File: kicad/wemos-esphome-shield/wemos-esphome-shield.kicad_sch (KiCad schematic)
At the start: 27 parts, among them Q1 2N2219, Q2 2N2219, Q3 2N2219, T1 Transformer_1P_1S, U1 WeMos_D1_mini

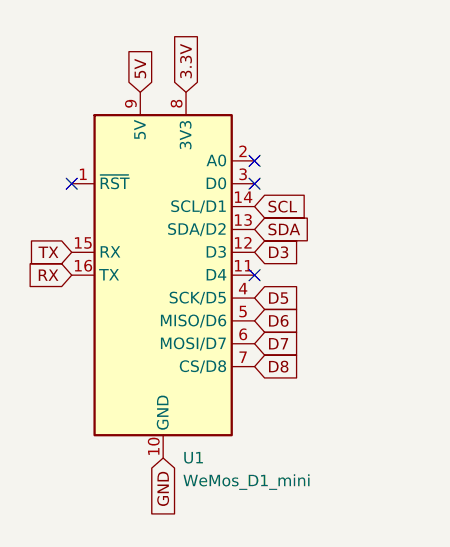
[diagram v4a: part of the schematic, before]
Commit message: first positioning of footprints
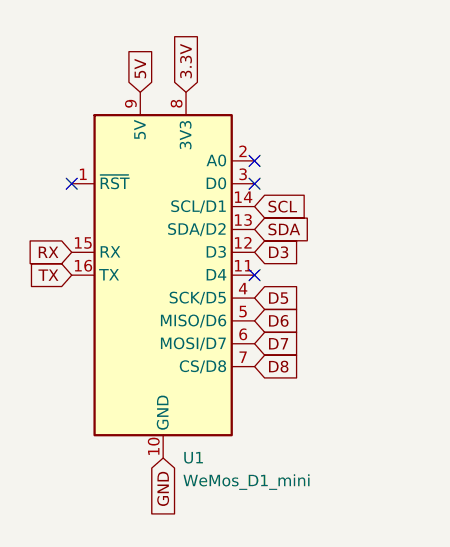
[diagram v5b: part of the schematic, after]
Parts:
- GEST1: footprint (none) -> internal:APDS9960
- LED1: footprint internal:LED ring -> internal:LED breakout
- LUM1: footprint internal:TEMT6000 -> internal:BH1750
- MOV1: footprint (none) -> internal:LD2410C
- OLED2: footprint internal:SSD1306 OLED 128x32 -> internal:SSD1306 OLED 128x64
- Q1, Q2, Q3: footprint Package_TO_SOT_THT:TO-92L_Inline -> Package_TO_SOT_SMD:SOT-23_Handsoldering
- R1, R5: footprint Resistor_THT:R_Axial_DIN0207_L6.3mm_D2.5mm_P10.16mm_Horizontal -> Resistor_SMD:R_1206_3216Metric_Pad1.30x1.75mm_HandSolder
- R2, R3, R4, R6, R7, R8: footprint (none) -> Resistor_SMD:R_1206_3216Metric_Pad1.30x1.75mm_HandSolder
- TEMP1: footprint Connector_JST:JST_XH_B4B-XH-AM_1x04_P2.50mm_Vertical -> Connector_JST:JST_XH_B4B-XH-A_1x04_P2.50mm_Vertical
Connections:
- net RX: now also U1.15 (RX); no longer U1.16 (TX)
- net TX: now also U1.16 (TX); no longer U1.15 (RX)
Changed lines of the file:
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@@
     )
   )
-  (global_label "TX" (shape input) (at 35.56 38.1 180) (fields_autoplaced)
-    (effects (font (size 1.27 1.27)) (justify right))
-    (property "Intersheetrefs" "${INTERSHEET_REFS}" (at 30.3977 38.1 0)
+  (global_label "TX" (shape input) (at 35.56 40.64 180) (fields_autoplaced)
+    (effects (font (size 1.27 1.27)) (justify right))
+    (property "Intersheetrefs" "${INTERSHEET_REFS}" (at 30.3977 40.64 0)
       (effects (font (size 1.27 1.27)) (justify right) hide)
     )
@@
     )
   )
-  (global_label "RX" (shape input) (at 35.56 40.64 180) (fields_autoplaced)
-    (effects (font (size 1.27 1.27)) (justify right))
-    (property "Intersheetrefs" "${INTERSHEET_REFS}" (at 30.0953 40.64 0)
+  (global_label "RX" (shape input) (at 35.56 38.1 180) (fields_autoplaced)
+    (effects (font (size 1.27 1.27)) (justify right))
+    (property "Intersheetrefs" "${INTERSHEET_REFS}" (at 30.0953 38.1 0)
       (effects (font (size 1.27 1.27)) (justify right) hide)
     )
@@
       (effects (font (size 1.27 1.27)) (justify right))
     )
-    (property "Footprint" "" (at 173.99 58.42 0)
+    (property "Footprint" "internal:LD2410C" (at 173.99 58.42 0)
       (effects (font (size 1.27 1.27)) hide)
     )
@@
       (effects (font (size 1.27 1.27)))
     )
-    (property "Footprint" "Resistor_THT:R_Axial_DIN0207_L6.3mm_D2.5mm_P10.16mm_Horizontal" (at 53.34 124.46 0)
+    (property "Footprint" "Resistor_SMD:R_1206_3216Metric_Pad1.30x1.75mm_HandSolder" (at 53.34 124.46 0)
       (effects (font (size 1.27 1.27)) hide)
     )
@@
       (effects (font (size 1.27 1.27)) (justify left))
     )
-    (property "Footprint" "Package_TO_SOT_THT:TO-92L_Inline" (at 76.2 126.365 0)
+    (property "Footprint" "Package_TO_SOT_SMD:SOT-23_Handsoldering" (at 76.2 126.365 0)
       (effects (font (size 1.27 1.27) italic) (justify left) hide)
     )
@@
       (effects (font (size 1.27 1.27)))
     )
-    (property "Footprint" "" (at 132.08 134.62 0)
+    (property "Footprint" "Resistor_SMD:R_1206_3216Metric_Pad1.30x1.75mm_HandSolder" (at 132.08 134.62 0)
       (effects (font (size 1.27 1.27)) hide)
     )
@@
       (effects (font (size 1.27 1.27)) (justify right))
     )
-    (property "Footprint" "" (at 198.12 63.5 0)
+    (property "Footprint" "internal:APDS9960" (at 198.12 63.5 0)
       (effects (font (size 1.27 1.27)) hide)
     )
@@
       (effects (font (size 1.27 1.27)))
     )
-    (property "Footprint" "" (at 62.23 97.79 0)
+    (property "Footprint" "Resistor_SMD:R_1206_3216Metric_Pad1.30x1.75mm_HandSolder" (at 62.23 97.79 0)
       (effects (font (size 1.27 1.27)) hide)
     )
@@
       (effects (font (size 1.27 1.27)))
     )
-    (property "Footprint" "" (at 124.46 124.46 0)
+    (property "Footprint" "Resistor_SMD:R_1206_3216Metric_Pad1.30x1.75mm_HandSolder" (at 124.46 124.46 0)
       (effects (font (size 1.27 1.27)) hide)
     )
@@
       (effects (font (size 1.27 1.27)))
     )
-    (property "Footprint" "" (at 125.73 109.22 0)
+    (property "Footprint" "Resistor_SMD:R_1206_3216Metric_Pad1.30x1.75mm_HandSolder" (at 125.73 109.22 0)
       (effects (font (size 1.27 1.27)) hide)
     )
@@
       (effects (font (size 1.27 1.27)))
     )
-    (property "Footprint" "Connector_JST:JST_XH_B4B-XH-AM_1x04_P2.50mm_Vertical" (at 173.99 77.47 0)
+    (property "Footprint" "Connector_JST:JST_XH_B4B-XH-A_1x04_P2.50mm_Vertical" (at 173.99 77.47 0)
       (effects (font (size 1.27 1.27)) hide)
     )
@@
       (effects (font (size 1.27 1.27)))
     )
-    (property "Footprint" "Resistor_THT:R_Axial_DIN0207_L6.3mm_D2.5mm_P10.16mm_Horizontal" (at 53.34 88.9 0)
+    (property "Footprint" "Resistor_SMD:R_1206_3216Metric_Pad1.30x1.75mm_HandSolder" (at 53.34 88.9 0)
       (effects (font (size 1.27 1.27)) hide)
     )
@@
       (effects (font (size 1.27 1.27)))
     )
-    (property "Footprint" "" (at 125.73 116.84 0)
+    (property "Footprint" "Resistor_SMD:R_1206_3216Metric_Pad1.30x1.75mm_HandSolder" (at 125.73 116.84 0)
       (effects (font (size 1.27 1.27)) hide)
     )
@@
       (effects (font (size 1.27 1.27)))
     )
-    (property "Footprint" "" (at 62.23 133.35 0)
+    (property "Footprint" "Resistor_SMD:R_1206_3216Metric_Pad1.30x1.75mm_HandSolder" (at 62.23 133.35 0)
       (effects (font (size 1.27 1.27)) hide)
     )
@@
       (effects (font (size 1.27 1.27)) (justify left))
     )
-    (property "Footprint" "Package_TO_SOT_THT:TO-92L_Inline" (at 76.2 90.805 0)
+    (property "Footprint" "Package_TO_SOT_SMD:SOT-23_Handsoldering" (at 76.2 90.805 0)
       (effects (font (size 1.27 1.27) italic) (justify left) hide)
     )
@@
       (effects (font (size 1.27 1.27)) (justify left))
     )
-    (property "Footprint" "Package_TO_SOT_THT:TO-92L_Inline" (at 139.7 126.365 0)
+    (property "Footprint" "Package_TO_SOT_SMD:SOT-23_Handsoldering" (at 139.7 126.365 0)
       (effects (font (size 1.27 1.27) italic) (justify left) hide)
     )
@@
       (effects (font (size 1.27 1.27)) (justify right))
     )
-    (property "Footprint" "internal:TEMT6000" (at 173.99 93.98 0)
+    (property "Footprint" "internal:BH1750" (at 173.99 93.98 0)
       (effects (font (size 1.27 1.27)) hide)
     )
@@
       (effects (font (size 1.27 1.27)) (justify right))
     )
-    (property "Footprint" "internal:SSD1306 OLED 128x32" (at 198.12 26.67 0)
+    (property "Footprint" "internal:SSD1306 OLED 128x64" (at 198.12 26.67 0)
       (effects (font (size 1.27 1.27)) hide)
     )
@@
       (effects (font (size 1.27 1.27)) (justify right))
     )
-    (property "Footprint" "internal:LED ring" (at 173.99 41.91 0)
-      (effects (font (size 1.27 1.27)) hide)
-    )
+    (property "Footprint" "internal:LED breakout" (at 173.99 41.91 0)
+      (effects (font (size 1.27 1.27)) hide)
+    )

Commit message: wire tracks
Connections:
- net 5V: now also OLED1.3 (Pin_3), OLED2.3 (Pin_3); no longer OLED1.2 (Pin_2), OLED2.2 (Pin_2)
- net GND: now also OLED1.4 (Pin_4), OLED2.4 (Pin_4); no longer OLED1.1 (Pin_1), OLED2.1 (Pin_1)
- net SCL: now also OLED1.2 (Pin_2), OLED2.2 (Pin_2); no longer OLED1.3 (Pin_3), OLED2.3 (Pin_3)
- net SDA: now also OLED1.1 (Pin_1), OLED2.1 (Pin_1); no longer OLED1.4 (Pin_4), OLED2.4 (Pin_4)
- net D8: no longer names the net of U1.7 (CS/D8)
- no-connect marks 9 -> 10
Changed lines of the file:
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@@
   (no_connect (at 55.88 40.64))
   (no_connect (at 55.88 30.48))
+  (no_connect (at 55.88 50.8))
   (no_connect (at 193.04 68.58))
   (no_connect (at 193.04 55.88))
@@
     )
   )
-  (global_label "D8" (shape input) (at 55.88 50.8 0) (fields_autoplaced)
-    (effects (font (size 1.27 1.27)) (justify left))
-    (property "Intersheetrefs" "${INTERSHEET_REFS}" (at 61.3447 50.8 0)
-      (effects (font (size 1.27 1.27)) (justify left) hide)
-    )
-  )
-  (global_label "SCL" (shape input) (at 193.04 24.13 180) (fields_autoplaced)
-    (effects (font (size 1.27 1.27)) (justify right))
-    (property "Intersheetrefs" "${INTERSHEET_REFS}" (at 187.1193 24.2094 0)
+  (global_label "SCL" (shape input) (at 193.04 26.67 180) (fields_autoplaced)
+    (effects (font (size 1.27 1.27)) (justify right))
+    (property "Intersheetrefs" "${INTERSHEET_REFS}" (at 187.1193 26.7494 0)
       (effects (font (size 1.27 1.27)) (justify right) hide)
     )
@@
     )
   )
-  (global_label "5V" (shape input) (at 193.04 26.67 180) (fields_autoplaced)
-    (effects (font (size 1.27 1.27)) (justify right))
-    (property "Intersheetrefs" "${INTERSHEET_REFS}" (at 188.3288 26.5906 0)
-      (effects (font (size 1.27 1.27)) (justify right) hide)
-    )
-  )
-  (global_label "SDA" (shape input) (at 168.91 21.59 180) (fields_autoplaced)
-    (effects (font (size 1.27 1.27)) (justify right))
-    (property "Intersheetrefs" "${INTERSHEET_REFS}" (at 162.9288 21.6694 0)
+  (global_label "5V" (shape input) (at 193.04 24.13 180) (fields_autoplaced)
+    (effects (font (size 1.27 1.27)) (justify right))
+    (property "Intersheetrefs" "${INTERSHEET_REFS}" (at 188.3288 24.0506 0)
+      (effects (font (size 1.27 1.27)) (justify right) hide)
+    )
+  )
+  (global_label "SDA" (shape input) (at 168.91 29.21 180) (fields_autoplaced)
+    (effects (font (size 1.27 1.27)) (justify right))
+    (property "Intersheetrefs" "${INTERSHEET_REFS}" (at 162.9288 29.2894 0)
       (effects (font (size 1.27 1.27)) (justify right) hide)
     )
@@
     )
   )
-  (global_label "GND" (shape input) (at 193.04 29.21 180) (fields_autoplaced)
-    (effects (font (size 1.27 1.27)) (justify right))
-    (property "Intersheetrefs" "${INTERSHEET_REFS}" (at 186.7564 29.1306 0)
+  (global_label "GND" (shape input) (at 193.04 21.59 180) (fields_autoplaced)
+    (effects (font (size 1.27 1.27)) (justify right))
+    (property "Intersheetrefs" "${INTERSHEET_REFS}" (at 186.7564 21.5106 0)
       (effects (font (size 1.27 1.27)) (justify right) hide)
     )
@@
     )
   )
-  (global_label "SDA" (shape input) (at 193.04 21.59 180) (fields_autoplaced)
-    (effects (font (size 1.27 1.27)) (justify right))
-    (property "Intersheetrefs" "${INTERSHEET_REFS}" (at 187.0588 21.6694 0)
+  (global_label "SDA" (shape input) (at 193.04 29.21 180) (fields_autoplaced)
+    (effects (font (size 1.27 1.27)) (justify right))
+    (property "Intersheetrefs" "${INTERSHEET_REFS}" (at 187.0588 29.2894 0)
       (effects (font (size 1.27 1.27)) (justify right) hide)
     )
@@
     )
   )
-  (global_label "GND" (shape input) (at 168.91 29.21 180) (fields_autoplaced)
-    (effects (font (size 1.27 1.27)) (justify right))
-    (property "Intersheetrefs" "${INTERSHEET_REFS}" (at 162.6264 29.1306 0)
+  (global_label "GND" (shape input) (at 168.91 21.59 180) (fields_autoplaced)
+    (effects (font (size 1.27 1.27)) (justify right))
+    (property "Intersheetrefs" "${INTERSHEET_REFS}" (at 162.6264 21.5106 0)
       (effects (font (size 1.27 1.27)) (justify right) hide)
     )
@@
     )
   )
-  (global_label "5V" (shape input) (at 168.91 26.67 180) (fields_autoplaced)
-    (effects (font (size 1.27 1.27)) (justify right))
-    (property "Intersheetrefs" "${INTERSHEET_REFS}" (at 164.1988 26.5906 0)
-      (effects (font (size 1.27 1.27)) (justify right) hide)
-    )
-  )
-  (global_label "SCL" (shape input) (at 168.91 24.13 180) (fields_autoplaced)
-    (effects (font (size 1.27 1.27)) (justify right))
-    (property "Intersheetrefs" "${INTERSHEET_REFS}" (at 162.9893 24.2094 0)
-      (effects (font (size 1.27 1.27)) (justify right) hide)
-    )
+  (global_label "5V" (shape input) (at 168.91 24.13 180) (fields_autoplaced)
+    (effects (font (size 1.27 1.27)) (justify right))
+    (property "Intersheetrefs" "${INTERSHEET_REFS}" (at 164.1988 24.0506 0)
+      (effects (font (size 1.27 1.27)) (justify right) hide)
+    )
+  )
+  (global_label "SCL" (shape input) (at 168.91 26.67 180) (fields_autoplaced)
+    (effects (font (size 1.27 1.27)) (justify right))
+    (property "Intersheetrefs" "${INTERSHEET_REFS}" (at 162.9893 26.7494 0)
+      (effects (font (size 1.27 1.27)) (justify right) hide)
+    )

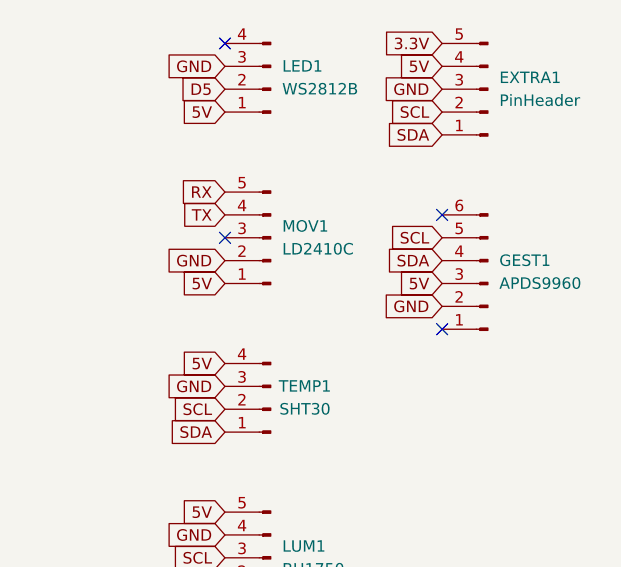
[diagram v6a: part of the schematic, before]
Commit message: route gesture sensor to 3.3v power
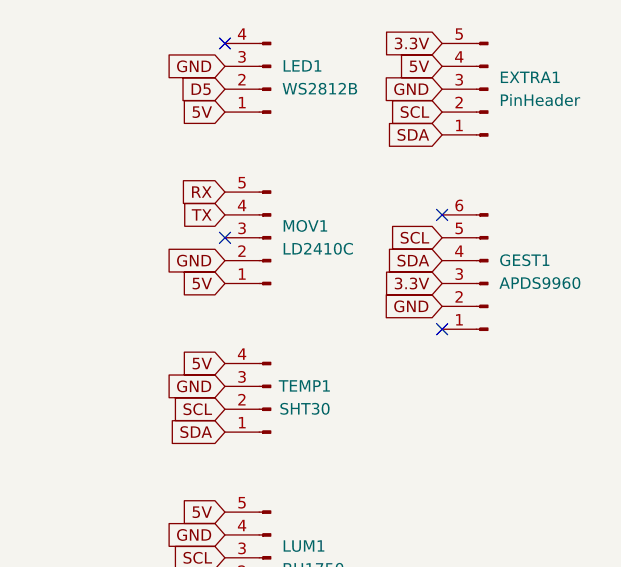
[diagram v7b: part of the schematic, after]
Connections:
- net 3.3V: now also GEST1.3 (Pin_3)
- net 5V: no longer GEST1.3 (Pin_3)
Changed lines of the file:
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@@
-    )
-  )
-  (global_label "5V" (shape input) (at 193.04 63.5 180) (fields_autoplaced)
-    (effects (font (size 1.27 1.27)) (justify right))
-    (property "Intersheetrefs" "${INTERSHEET_REFS}" (at 188.3288 63.4206 0)
-      (effects (font (size 1.27 1.27)) (justify right) hide)
     )
   )
@@
       (effects (font (size 1.27 1.27)) (justify right) hide)
     )
+  )
+  (global_label "3.3V" (shape input) (at 193.04 63.5 180) (fields_autoplaced)
+    (effects (font (size 1.27 1.27)) (justify right))
+    (property "Intersheetrefs" "${INTERSHEET_REFS}" (at 185.9424 63.5 0)
+      (effects (font (size 1.27 1.27)) (justify right) hide)
+    )

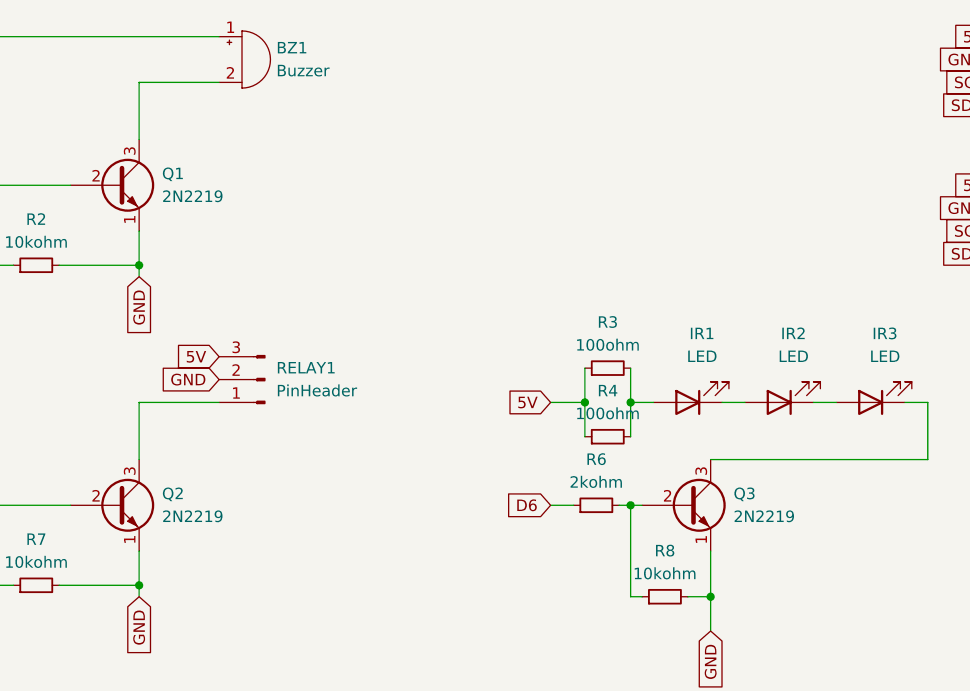
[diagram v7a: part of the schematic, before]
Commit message: custom SOT-23 footprint and other small adjustments
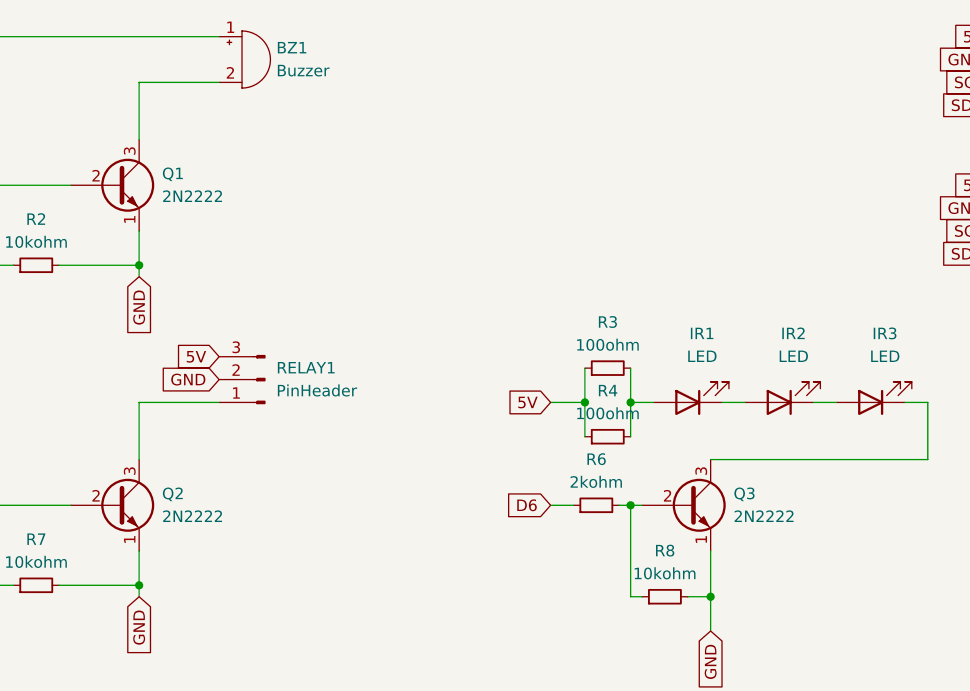
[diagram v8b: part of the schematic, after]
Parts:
- Q1, Q2, Q3: value 2N2219 -> 2N2222; footprint Package_TO_SOT_SMD:SOT-23_Handsoldering -> internal:SOT-23_Handsoldering
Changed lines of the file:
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@@
   (symbol (lib_id "Transistor_BJT:2N2219") (at 71.12 124.46 0) (unit 1)
     (in_bom yes) (on_board yes) (dnp no) (fields_autoplaced)
-    (property "Reference" "Q2" (at 76.2 123.1899 0)
-      (effects (font (size 1.27 1.27)) (justify left))
-    )
-    (property "Value" "2N2219" (at 76.2 125.7299 0)
-      (effects (font (size 1.27 1.27)) (justify left))
-    )
-    (property "Footprint" "Package_TO_SOT_SMD:SOT-23_Handsoldering" (at 76.2 126.365 0)
+    (property "Reference" "Q2" (at 76.2 123.19 0)
+      (effects (font (size 1.27 1.27)) (justify left))
+    )
+    (property "Value" "2N2222" (at 76.2 125.73 0)
+      (effects (font (size 1.27 1.27)) (justify left))
+    )
+    (property "Footprint" "internal:SOT-23_Handsoldering" (at 76.2 126.365 0)
       (effects (font (size 1.27 1.27) italic) (justify left) hide)
     )
@@
   (symbol (lib_id "Transistor_BJT:2N2219") (at 71.12 88.9 0) (unit 1)
     (in_bom yes) (on_board yes) (dnp no) (fields_autoplaced)
-    (property "Reference" "Q1" (at 76.2 87.6299 0)
-      (effects (font (size 1.27 1.27)) (justify left))
-    )
-    (property "Value" "2N2219" (at 76.2 90.1699 0)
-      (effects (font (size 1.27 1.27)) (justify left))
-    )
-    (property "Footprint" "Package_TO_SOT_SMD:SOT-23_Handsoldering" (at 76.2 90.805 0)
+    (property "Reference" "Q1" (at 76.2 87.63 0)
+      (effects (font (size 1.27 1.27)) (justify left))
+    )
+    (property "Value" "2N2222" (at 76.2 90.17 0)
+      (effects (font (size 1.27 1.27)) (justify left))
+    )
+    (property "Footprint" "internal:SOT-23_Handsoldering" (at 76.2 90.805 0)
       (effects (font (size 1.27 1.27) italic) (justify left) hide)
     )
@@
   (symbol (lib_id "Transistor_BJT:2N2219") (at 134.62 124.46 0) (unit 1)
     (in_bom yes) (on_board yes) (dnp no) (fields_autoplaced)
-    (property "Reference" "Q3" (at 139.7 123.1899 0)
-      (effects (font (size 1.27 1.27)) (justify left))
-    )
-    (property "Value" "2N2219" (at 139.7 125.7299 0)
-      (effects (font (size 1.27 1.27)) (justify left))
-    )
-    (property "Footprint" "Package_TO_SOT_SMD:SOT-23_Handsoldering" (at 139.7 126.365 0)
+    (property "Reference" "Q3" (at 139.7 123.19 0)
+      (effects (font (size 1.27 1.27)) (justify left))
+    )
+    (property "Value" "2N2222" (at 139.7 125.73 0)
+      (effects (font (size 1.27 1.27)) (justify left))
+    )
+    (property "Footprint" "internal:SOT-23_Handsoldering" (at 139.7 126.365 0)
       (effects (font (size 1.27 1.27) italic) (justify left) hide)
     )
